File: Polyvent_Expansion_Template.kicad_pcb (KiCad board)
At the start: 2 copper layers, 100 x 80 mm, 5 parts, among them J1 09231486921

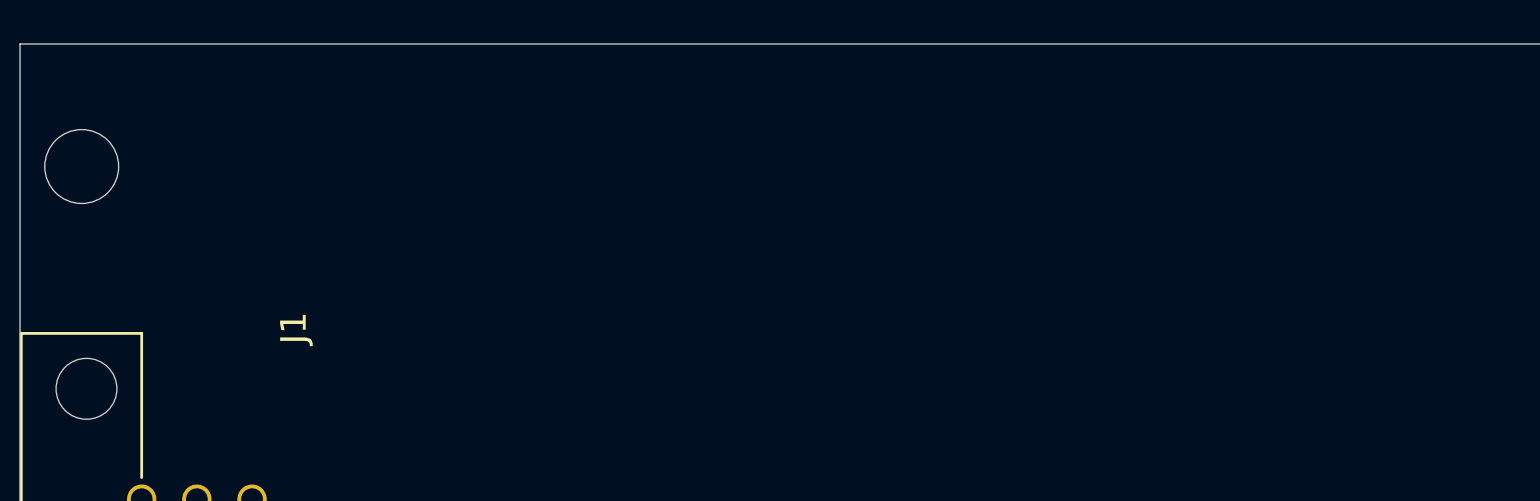
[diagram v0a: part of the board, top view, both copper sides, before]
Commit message: Add defaults to schematic and PCB including license and Public Invetion Name. Lock the connector on PCB.
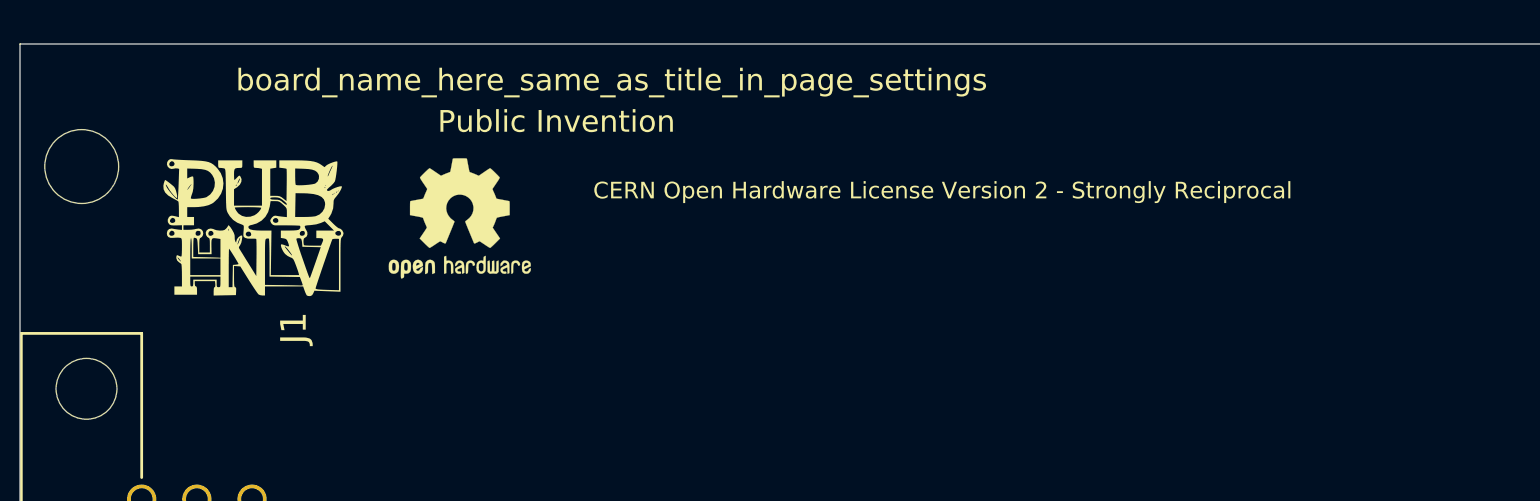
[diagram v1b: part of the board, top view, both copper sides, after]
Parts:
- added G***: LOGO, PubInv_PCB:Logo_PI_BandW_70percent_10x10, F.Cu at (109.2, 73.7)
- added Graphic1: OSHW-Logo2_7.3x6mm_SilkScreen, Symbol:OSHW-Logo2_7.3x6mm_SilkScreen, F.Cu at (118.7, 73.0)
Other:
- board text added: "CERN Open Hardware License Version 2 - Strongly Reciprocal"
- board text added: "Public Invention"
- board text added: "board_name_here_same_as_title_in_page_settings"
